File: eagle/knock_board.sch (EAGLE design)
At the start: 13 parts, among them U2 TLC2262CP, U3 ATTINY25V-10PU

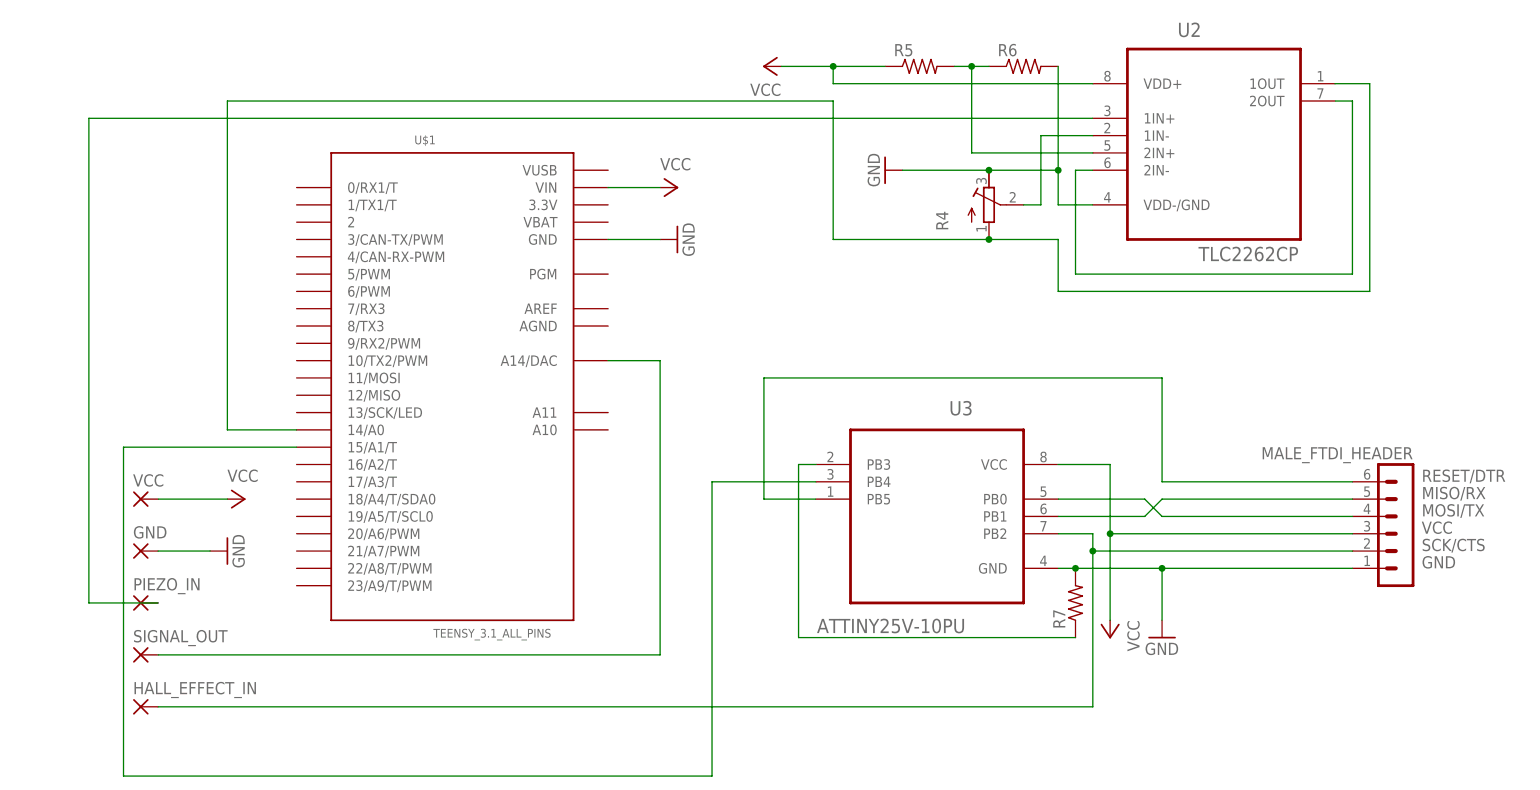
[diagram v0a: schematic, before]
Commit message: clean up schematic
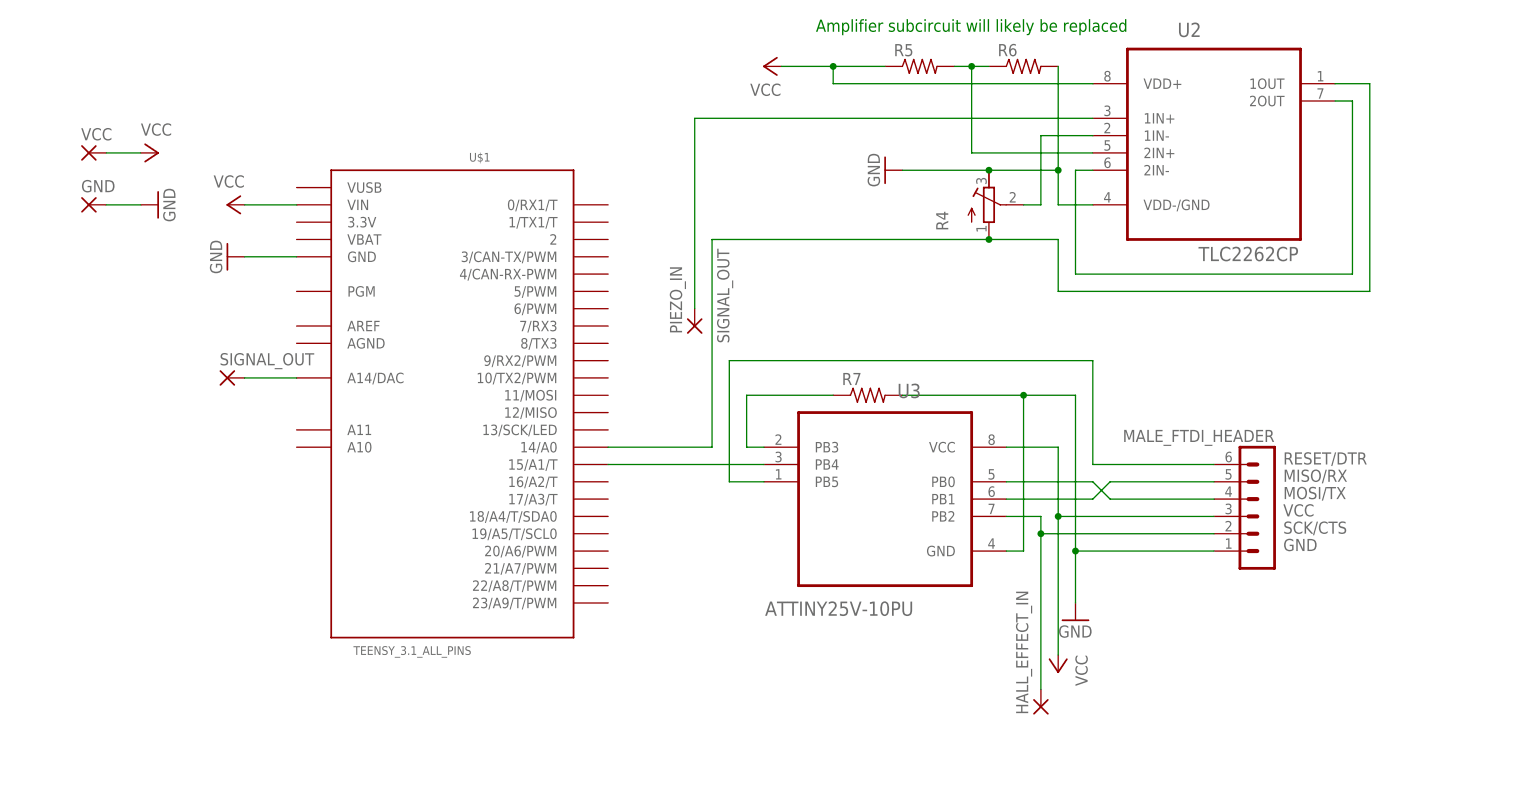
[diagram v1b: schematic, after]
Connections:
- net SIGNAL_IN renamed N$2
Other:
- note added: "Amplifier subcircuit will likely be replaced"
- moved on the sheet: GND, HALL_EFFECT_IN, MALE_FTDI_HEADER, PIEZO_IN, R7, SIGNAL_OUT, U$1, U3, VCC

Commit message: added diagnostic LEDs
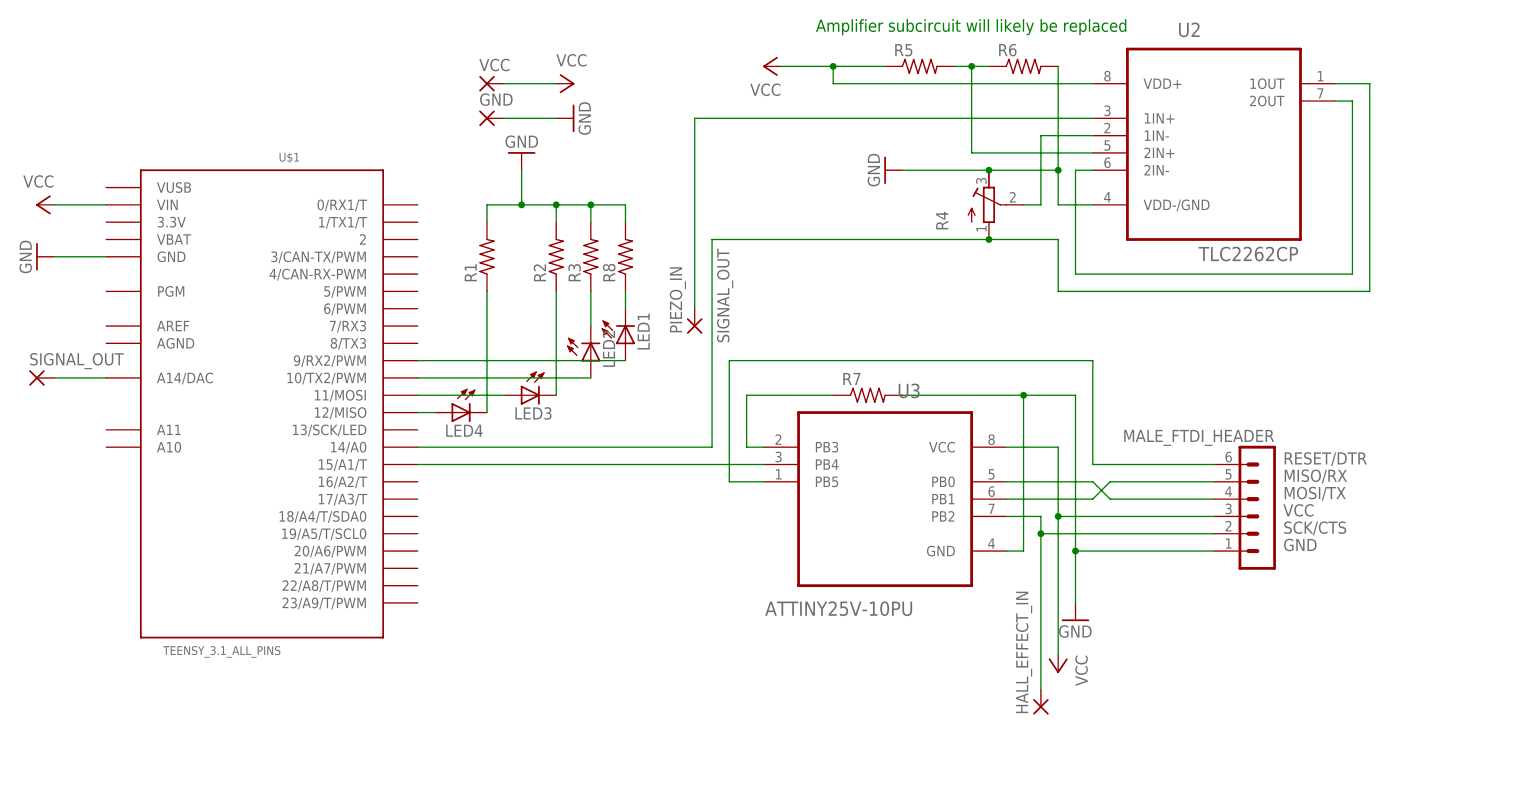
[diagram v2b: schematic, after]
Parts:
- added LED1, LED2, LED3, LED4: (no value), led:LED3MM
- added R1, R2, R3, R8: (no value), rcl:R-US_0204/5
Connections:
- new net N$10: LED1.A, U$1.9/RX2/PWM
- new net N$11: LED4.C, R1.1
- new net N$12: LED3.C, R2.1
- new net N$13: LED2.C, R3.1
- new net N$14: LED1.C, R8.1
- new net N$5: LED4.A, U$1.12/MISO
- new net N$8: LED3.A, U$1.11/MOSI
- new net N$9: LED2.A, U$1.10/TX2/PWM
- net GND: now also R1.2, R2.2, R3.2, R8.2
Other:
- moved on the sheet: GND, SIGNAL_OUT, U$1, VCC
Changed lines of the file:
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@@
 <part name="P+4" library="supply1" deviceset="VCC" device=""/>
 <part name="GND4" library="supply1" deviceset="GND" device=""/>
+<part name="LED1" library="led" deviceset="LED" device="3MM"/>
+<part name="LED2" library="led" deviceset="LED" device="3MM"/>
+<part name="LED3" library="led" deviceset="LED" device="3MM"/>
+<part name="LED4" library="led" deviceset="LED" device="3MM"/>
+<part name="R1" library="rcl" deviceset="R-US_" device="0204/5"/>
+<part name="R2" library="rcl" deviceset="R-US_" device="0204/5"/>
+<part name="R3" library="rcl" deviceset="R-US_" device="0204/5"/>
+<part name="R8" library="rcl" deviceset="R-US_" device="0204/5"/>
+<part name="GND5" library="supply1" deviceset="GND" device=""/>
 </parts>
 <sheets>
@@
 <instance part="R5" gate="G$1" x="104.14" y="137.16"/>
 <instance part="R6" gate="G$1" x="119.38" y="137.16"/>
-<instance part="U$1" gate="G$1" x="35.56" y="88.9" rot="MR0"/>
-<instance part="VCC" gate="1" x="-17.78" y="124.46"/>
-<instance part="GND" gate="1" x="-17.78" y="116.84"/>
+<instance part="U$1" gate="G$1" x="7.62" y="88.9" rot="MR0"/>
+<instance part="VCC" gate="1" x="40.64" y="134.62"/>
+<instance part="GND" gate="1" x="40.64" y="129.54"/>
 <instance part="PIEZO_IN" gate="1" x="71.12" y="99.06" rot="R90"/>
 <instance part="HALL_EFFECT_IN" gate="1" x="121.92" y="43.18" rot="R90"/>
-<instance part="SIGNAL_OUT" gate="1" x="2.54" y="91.44"/>
+<instance part="SIGNAL_OUT" gate="1" x="-25.4" y="91.44"/>
 <instance part="MALE_FTDI_HEADER" gate="1" x="154.94" y="73.66" rot="MR0"/>
-<instance part="P+1" gate="VCC" x="-7.62" y="124.46" rot="R270"/>
+<instance part="P+1" gate="VCC" x="53.34" y="134.62" rot="R270"/>
 <instance part="P+2" gate="VCC" x="81.28" y="137.16" rot="R90"/>
 <instance part="P+3" gate="VCC" x="124.46" y="48.26" rot="R180"/>
 <instance part="GND1" gate="1" x="127" y="55.88"/>
 <instance part="GND2" gate="1" x="99.06" y="121.92" rot="R270"/>
-<instance part="GND3" gate="1" x="-7.62" y="116.84" rot="R90"/>
-<instance part="P+4" gate="VCC" x="2.54" y="116.84" rot="MR270"/>
-<instance part="GND4" gate="1" x="2.54" y="109.22" rot="MR90"/>
+<instance part="GND3" gate="1" x="53.34" y="129.54" rot="R90"/>
+<instance part="P+4" gate="VCC" x="-25.4" y="116.84" rot="MR270"/>
+<instance part="GND4" gate="1" x="-25.4" y="109.22" rot="MR90"/>
+<instance part="LED1" gate="G$1" x="60.96" y="96.52" rot="MR180"/>
+<instance part="LED2" gate="G$1" x="55.88" y="93.98" rot="MR180"/>
+<instance part="LED3" gate="G$1" x="45.72" y="88.9" rot="MR270"/>
+<instance part="LED4" gate="G$1" x="35.56" y="86.36" rot="MR270"/>
+<instance part="R1" gate="G$1" x="40.64" y="109.22" rot="R90"/>
+<instance part="R2" gate="G$1" x="50.8" y="109.22" rot="R90"/>
+<instance part="R3" gate="G$1" x="55.88" y="109.22" rot="R90"/>
+<instance part="R8" gate="G$1" x="60.96" y="109.22" rot="R90"/>
+<instance part="GND5" gate="1" x="45.72" y="124.46" rot="R180"/>
 </instances>
 <busses>
@@
 <segment>
 <pinref part="U3" gate="A" pin="PB4"/>
-<wire x1="81.28" y1="78.74" x2="58.42" y2="78.74" width="0.1524" layer="91"/>
+<wire x1="81.28" y1="78.74" x2="30.48" y2="78.74" width="0.1524" layer="91"/>
 <pinref part="U$1" gate="G$1" pin="15/A1/T"/>
 </segment>
@@
 <pinref part="GND" gate="1" pin="P"/>
 <pinref part="GND3" gate="1" pin="GND"/>
-<wire x1="-15.24" y1="116.84" x2="-10.16" y2="116.84" width="0.1524" layer="91"/>
+<wire x1="43.18" y1="129.54" x2="50.8" y2="129.54" width="0.1524" layer="91"/>
 </segment>
 <segment>
 <pinref part="GND4" gate="1" pin="GND"/>
 <pinref part="U$1" gate="G$1" pin="GND"/>
-<wire x1="5.08" y1="109.22" x2="12.7" y2="109.22" width="0.1524" layer="91"/>
+<wire x1="-22.86" y1="109.22" x2="-15.24" y2="109.22" width="0.1524" layer="91"/>
+</segment>
+<segment>
+<pinref part="R1" gate="G$1" pin="2"/>
+<wire x1="40.64" y1="114.3" x2="40.64" y2="116.84" width="0.1524" layer="91"/>
+<wire x1="40.64" y1="116.84" x2="45.72" y2="116.84" width="0.1524" layer="91"/>
+<pinref part="R2" gate="G$1" pin="2"/>
+<wire x1="45.72" y1="116.84" x2="50.8" y2="116.84" width="0.1524" layer="91"/>
+<wire x1="50.8" y1="116.84" x2="50.8" y2="114.3" width="0.1524" layer="91"/>
+<wire x1="50.8" y1="116.84" x2="55.88" y2="116.84" width="0.1524" layer="91"/>
+<junction x="50.8" y="116.84"/>
+<pinref part="R3" gate="G$1" pin="2"/>
+<wire x1="55.88" y1="116.84" x2="55.88" y2="114.3" width="0.1524" layer="91"/>
+<wire x1="55.88" y1="116.84" x2="60.96" y2="116.84" width="0.1524" layer="91"/>
+<junction x="55.88" y="116.84"/>
+<pinref part="R8" gate="G$1" pin="2"/>
+<wire x1="60.96" y1="116.84" x2="60.96" y2="114.3" width="0.1524" layer="91"/>
+<wire x1="45.72" y1="116.84" x2="45.72" y2="121.92" width="0.1524" layer="91"/>
+<junction x="45.72" y="116.84"/>
+<pinref part="GND5" gate="1" pin="GND"/>
 </segment>
 </net>
@@
 <pinref part="VCC" gate="1" pin="P"/>
 <pinref part="P+1" gate="VCC" pin="VCC"/>
-<wire x1="-15.24" y1="124.46" x2="-10.16" y2="124.46" width="0.1524" layer="91"/>
+<wire x1="43.18" y1="134.62" x2="50.8" y2="134.62" width="0.1524" layer="91"/>
 </segment>
 <segment>
 <pinref part="P+4" gate="VCC" pin="VCC"/>
 <pinref part="U$1" gate="G$1" pin="VIN"/>
-<wire x1="5.08" y1="116.84" x2="12.7" y2="116.84" width="0.1524" layer="91"/>
+<wire x1="-22.86" y1="116.84" x2="-15.24" y2="116.84" width="0.1524" layer="91"/>
 </segment>
 </net>
@@
 <junction x="114.3" y="111.76"/>
 <pinref part="U$1" gate="G$1" pin="14/A0"/>
-<wire x1="73.66" y1="81.28" x2="58.42" y2="81.28" width="0.1524" layer="91"/>
+<wire x1="73.66" y1="81.28" x2="30.48" y2="81.28" width="0.1524" layer="91"/>
 <wire x1="73.66" y1="81.28" x2="73.66" y2="111.76" width="0.1524" layer="91"/>
 <wire x1="73.66" y1="111.76" x2="114.3" y2="111.76" width="0.1524" layer="91"/>
@@
 <pinref part="SIGNAL_OUT" gate="1" pin="P"/>
 <pinref part="U$1" gate="G$1" pin="A14/DAC"/>
-<wire x1="5.08" y1="91.44" x2="12.7" y2="91.44" width="0.1524" layer="91"/>
+<wire x1="-22.86" y1="91.44" x2="-15.24" y2="91.44" width="0.1524" layer="91"/>
 </segment>
 </net>
@@
 </segment>
 </net>
+<net name="N$5" class="0">
+<segment>
+<pinref part="U$1" gate="G$1" pin="12/MISO"/>
+<pinref part="LED4" gate="G$1" pin="A"/>
+<wire x1="30.48" y1="86.36" x2="33.02" y2="86.36" width="0.1524" layer="91"/>
+</segment>
+</net>
+<net name="N$8" class="0">
+<segment>
+<pinref part="U$1" gate="G$1" pin="11/MOSI"/>
+<pinref part="LED3" gate="G$1" pin="A"/>
+<wire x1="30.48" y1="88.9" x2="43.18" y2="88.9" width="0.1524" layer="91"/>
+</segment>
+</net>
+<net name="N$9" class="0">
+<segment>
+<pinref part="U$1" gate="G$1" pin="10/TX2/PWM"/>
+<pinref part="LED2" gate="G$1" pin="A"/>
+<wire x1="30.48" y1="91.44" x2="55.88" y2="91.44" width="0.1524" layer="91"/>
+</segment>
+</net>
+<net name="N$10" class="0">
+<segment>
+<pinref part="U$1" gate="G$1" pin="9/RX2/PWM"/>
+<pinref part="LED1" gate="G$1" pin="A"/>
+<wire x1="30.48" y1="93.98" x2="60.96" y2="93.98" width="0.1524" layer="91"/>
+</segment>
+</net>
+<net name="N$11" class="0">
+<segment>
+<pinref part="LED4" gate="G$1" pin="C"/>
+<pinref part="R1" gate="G$1" pin="1"/>
+<wire x1="40.64" y1="86.36" x2="40.64" y2="104.14" width="0.1524" layer="91"/>
+</segment>
+</net>
+<net name="N$12" class="0">
+<segment>
+<pinref part="LED3" gate="G$1" pin="C"/>
+<pinref part="R2" gate="G$1" pin="1"/>
+<wire x1="50.8" y1="88.9" x2="50.8" y2="104.14" width="0.1524" layer="91"/>
+</segment>
+</net>
+<net name="N$13" class="0">
+<segment>
+<pinref part="LED2" gate="G$1" pin="C"/>
+<pinref part="R3" gate="G$1" pin="1"/>
+<wire x1="55.88" y1="99.06" x2="55.88" y2="104.14" width="0.1524" layer="91"/>
+</segment>
+</net>
+<net name="N$14" class="0">
+<segment>
+<pinref part="LED1" gate="G$1" pin="C"/>
+<pinref part="R8" gate="G$1" pin="1"/>
+<wire x1="60.96" y1="101.6" x2="60.96" y2="104.14" width="0.1524" layer="91"/>
+</segment>
+</net>

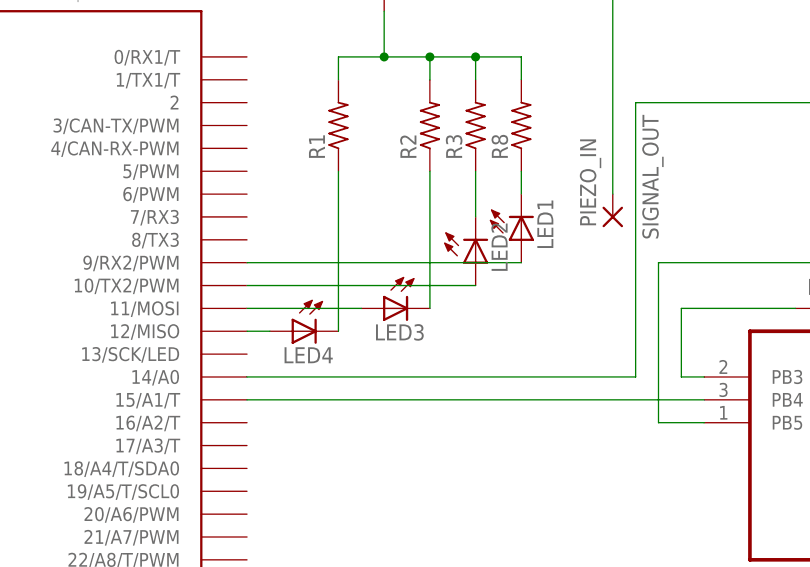
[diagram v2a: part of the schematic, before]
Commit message: add teensy project folder
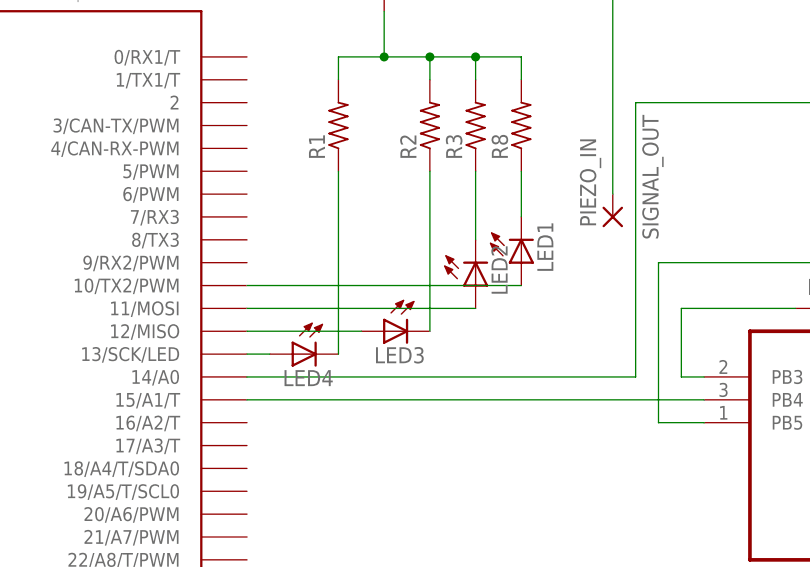
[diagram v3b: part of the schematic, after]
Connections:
- net N$10: now also U$1.10/TX2/PWM; no longer U$1.9/RX2/PWM
- net N$5: now also U$1.13/SCK/LED; no longer U$1.12/MISO
- net N$8: now also U$1.12/MISO; no longer U$1.11/MOSI
- net N$9: now also U$1.11/MOSI; no longer U$1.10/TX2/PWM
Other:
- moved on the sheet: LED1, LED2, LED3, LED4
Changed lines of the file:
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@@
 <instance part="P+4" gate="VCC" x="-25.4" y="116.84" rot="MR270"/>
 <instance part="GND4" gate="1" x="-25.4" y="109.22" rot="MR90"/>
-<instance part="LED1" gate="G$1" x="60.96" y="96.52" rot="MR180"/>
-<instance part="LED2" gate="G$1" x="55.88" y="93.98" rot="MR180"/>
-<instance part="LED3" gate="G$1" x="45.72" y="88.9" rot="MR270"/>
-<instance part="LED4" gate="G$1" x="35.56" y="86.36" rot="MR270"/>
+<instance part="LED1" gate="G$1" x="60.96" y="93.98" rot="MR180"/>
+<instance part="LED2" gate="G$1" x="55.88" y="91.44" rot="MR180"/>
+<instance part="LED3" gate="G$1" x="45.72" y="86.36" rot="MR270"/>
+<instance part="LED4" gate="G$1" x="35.56" y="83.82" rot="MR270"/>
 <instance part="R1" gate="G$1" x="40.64" y="109.22" rot="R90"/>
 <instance part="R2" gate="G$1" x="50.8" y="109.22" rot="R90"/>
@@
 </segment>
 </net>
-<net name="N$5" class="0">
-<segment>
-<pinref part="U$1" gate="G$1" pin="12/MISO"/>
-<pinref part="LED4" gate="G$1" pin="A"/>
-<wire x1="30.48" y1="86.36" x2="33.02" y2="86.36" width="0.1524" layer="91"/>
-</segment>
-</net>
-<net name="N$8" class="0">
-<segment>
-<pinref part="U$1" gate="G$1" pin="11/MOSI"/>
-<pinref part="LED3" gate="G$1" pin="A"/>
-<wire x1="30.48" y1="88.9" x2="43.18" y2="88.9" width="0.1524" layer="91"/>
-</segment>
-</net>
-<net name="N$9" class="0">
-<segment>
-<pinref part="U$1" gate="G$1" pin="10/TX2/PWM"/>
-<pinref part="LED2" gate="G$1" pin="A"/>
-<wire x1="30.48" y1="91.44" x2="55.88" y2="91.44" width="0.1524" layer="91"/>
-</segment>
-</net>
-<net name="N$10" class="0">
-<segment>
-<pinref part="U$1" gate="G$1" pin="9/RX2/PWM"/>
-<pinref part="LED1" gate="G$1" pin="A"/>
-<wire x1="30.48" y1="93.98" x2="60.96" y2="93.98" width="0.1524" layer="91"/>
-</segment>
-</net>
 <net name="N$11" class="0">
 <segment>
 <pinref part="LED4" gate="G$1" pin="C"/>
 <pinref part="R1" gate="G$1" pin="1"/>
-<wire x1="40.64" y1="86.36" x2="40.64" y2="104.14" width="0.1524" layer="91"/>
+<wire x1="40.64" y1="83.82" x2="40.64" y2="104.14" width="0.1524" layer="91"/>
 </segment>
 </net>
@@
 <pinref part="LED3" gate="G$1" pin="C"/>
 <pinref part="R2" gate="G$1" pin="1"/>
-<wire x1="50.8" y1="88.9" x2="50.8" y2="104.14" width="0.1524" layer="91"/>
+<wire x1="50.8" y1="86.36" x2="50.8" y2="104.14" width="0.1524" layer="91"/>
 </segment>
 </net>
@@
 <pinref part="LED2" gate="G$1" pin="C"/>
 <pinref part="R3" gate="G$1" pin="1"/>
-<wire x1="55.88" y1="99.06" x2="55.88" y2="104.14" width="0.1524" layer="91"/>
+<wire x1="55.88" y1="96.52" x2="55.88" y2="104.14" width="0.1524" layer="91"/>
 </segment>
 </net>
@@
 <pinref part="LED1" gate="G$1" pin="C"/>
 <pinref part="R8" gate="G$1" pin="1"/>
-<wire x1="60.96" y1="101.6" x2="60.96" y2="104.14" width="0.1524" layer="91"/>
-</segment>
-</net>
+<wire x1="60.96" y1="99.06" x2="60.96" y2="104.14" width="0.1524" layer="91"/>
+</segment>
+</net>
+<net name="N$5" class="0">
+<segment>
+<pinref part="LED4" gate="G$1" pin="A"/>
+<pinref part="U$1" gate="G$1" pin="13/SCK/LED"/>
+<wire x1="33.02" y1="83.82" x2="30.48" y2="83.82" width="0.1524" layer="91"/>
+</segment>
+</net>
+<net name="N$8" class="0">
+<segment>
+<pinref part="U$1" gate="G$1" pin="12/MISO"/>
+<pinref part="LED3" gate="G$1" pin="A"/>
+<wire x1="30.48" y1="86.36" x2="43.18" y2="86.36" width="0.1524" layer="91"/>
+</segment>
+</net>
+<net name="N$9" class="0">
+<segment>
+<pinref part="U$1" gate="G$1" pin="11/MOSI"/>
+<pinref part="LED2" gate="G$1" pin="A"/>
+<wire x1="30.48" y1="88.9" x2="55.88" y2="88.9" width="0.1524" layer="91"/>
+</segment>
+</net>
+<net name="N$10" class="0">
+<segment>
+<pinref part="LED1" gate="G$1" pin="A"/>
+<pinref part="U$1" gate="G$1" pin="10/TX2/PWM"/>
+<wire x1="60.96" y1="91.44" x2="30.48" y2="91.44" width="0.1524" layer="91"/>
+</segment>
+</net>
